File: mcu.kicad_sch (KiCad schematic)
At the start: 17 parts, among them J2 Conn_ARM_SWD_TagConnect_TC2030, U3 STM32L053R8Tx

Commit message: Added plugged in detection
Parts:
- added R39: 10M, Resistor_SMD:R_0402_1005Metric, symbol Device:R
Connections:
- net VDD: now also R39.1
- net SOLAR_PLUG: now reaches U3.27 (PB1)
- net SOLAR_PLUG: now also R39.2
- no-connect marks 34 -> 33
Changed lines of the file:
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@@
+	)
+	(junction
+		(at 193.04 96.52)
+		(diameter 0)
+		(color 0 0 0 0)
 	)
 	(junction
@@
 	)
 	(no_connect
-		(at 158.75 96.52)
-	)
-	(no_connect
 		(at 68.58 41.91)
 	)
@@
 	(wire
 		(pts
+			(xy 158.75 96.52) (xy 193.04 96.52)
+		)
+		(stroke
+			(width 0)
+			(type default)
+		)
+	)
+	(wire
+		(pts
 			(xy 165.1 121.92) (xy 158.75 121.92)
 		)
@@
 		(pts
 			(xy 250.19 26.67) (xy 256.54 26.67)
+		)
+		(stroke
+			(width 0)
+			(type default)
+		)
+	)
+	(wire
+		(pts
+			(xy 193.04 96.52) (xy 196.85 96.52)
 		)
 		(stroke
@@
 		(property "Intersheetrefs" "${INTERSHEET_REFS}"
 			(at 180.9667 53.34 0)
+			(effects
+				(font
+					(size 1.27 1.27)
+				)
+				(justify left)
+				(hide yes)
+			)
+		)
+	)
+	(global_label "SOLAR_PLUG"
+		(shape input)
+		(at 196.85 96.52 0)
+		(fields_autoplaced yes)
+		(effects
+			(font
+				(size 1.27 1.27)
+			)
+			(justify left)
+		)
+		(property "Intersheetrefs" "${INTERSHEET_REFS}"
+			(at 211.6281 96.52 0)
 			(effects
 				(font
@@
 	)
 	(symbol
+		(lib_id "Device:R")
+		(at 193.04 92.71 0)
+		(unit 1)
+		(exclude_from_sim no)
+		(in_bom yes)
+		(on_board yes)
+		(dnp no)
+		(fields_autoplaced yes)
+		(property "Reference" "R39"
+			(at 195.58 91.4399 0)
+			(effects
+				(font
+					(size 1.27 1.27)
+				)
+				(justify left)
+			)
+		)
+		(property "Value" "10M"
+			(at 195.58 93.9799 0)
+			(effects
+				(font
+					(size 1.27 1.27)
+				)
+				(justify left)
+			)
+		)
+		(property "Footprint" "Resistor_SMD:R_0402_1005Metric"
+			(at 191.262 92.71 90)
+			(effects
+				(font
+					(size 1.27 1.27)
+				)
+				(hide yes)
+			)
+		)
+		(property "Datasheet" "~"
+			(at 193.04 92.71 0)
+			(effects
+				(font
+					(size 1.27 1.27)
+				)
+				(hide yes)
+			)
+		)
+		(property "Description" "Resistor"
+			(at 193.04 92.71 0)
+			(effects
+				(font
+					(size 1.27 1.27)
+				)
+				(hide yes)
+			)
+		)
+		(pin "1"
+		)
+		(pin "2"
+		)
+		(instances
+			(project "JPBms2"
+				(path "/d86e471c-a8be-422d-a5d1-5a4699b7b766/852788cb-2266-4d4a-865c-a7e0873e4190"
+					(reference "R39")
+					(unit 1)
+				)
+			)
+		)
+	)
+	(symbol
 		(lib_id "power:PWR_FLAG")
 		(at 148.59 41.91 270)
@@
 					(unit 1)
 				)
+			)
+		)
+	)
+	(symbol
+		(lib_id "power:VDD")
+		(at 193.04 88.9 0)
+		(unit 1)
+		(exclude_from_sim no)
+		(in_bom yes)
+		(on_board yes)
+		(dnp no)
+		(fields_autoplaced yes)
+		(property "Reference" "#PWR053"
+			(at 193.04 92.71 0)
+			(effects
+				(font
+					(size 1.27 1.27)
+				)
+				(hide yes)
+			)
+		)
+		(property "Value" "VDD"
+			(at 193.04 83.82 0)
+			(effects
+				(font
+					(size 1.27 1.27)
+				)
+			)
+		)
+		(property "Footprint" ""
+			(at 193.04 88.9 0)
+			(effects
+				(font
+					(size 1.27 1.27)
+				)
+				(hide yes)
+			)
+		)
+		(property "Datasheet" ""
+			(at 193.04 88.9 0)
+			(effects
+				(font
+					(size 1.27 1.27)
+				)
+				(hide yes)
+			)
+		)
+		(property "Description" "Power symbol creates a global label with name \"VDD\""
+			(at 193.04 88.9 0)
+			(effects
+				(font
+					(size 1.27 1.27)
+				)
+				(hide yes)
+			)
+		)
+		(pin "1"
+		)
+		(instances
+			(project "JPBms2"
+				(path "/d86e471c-a8be-422d-a5d1-5a4699b7b766/852788cb-2266-4d4a-865c-a7e0873e4190"
+					(reference "#PWR053")
+					(unit 1)
+				)

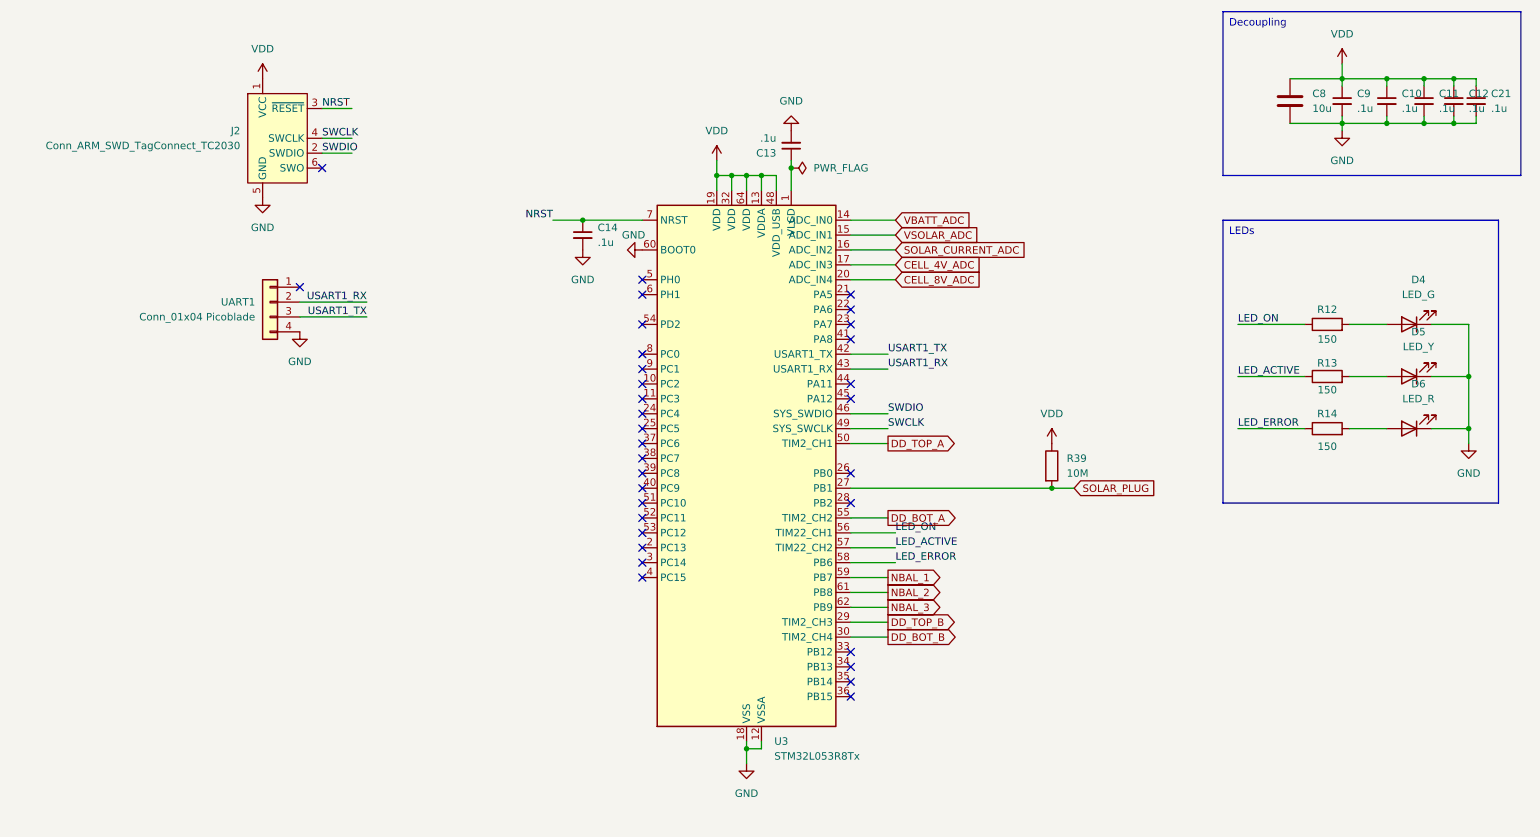
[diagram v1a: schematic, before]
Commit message: Adding a few notes, adding detection on solar and uart plugs
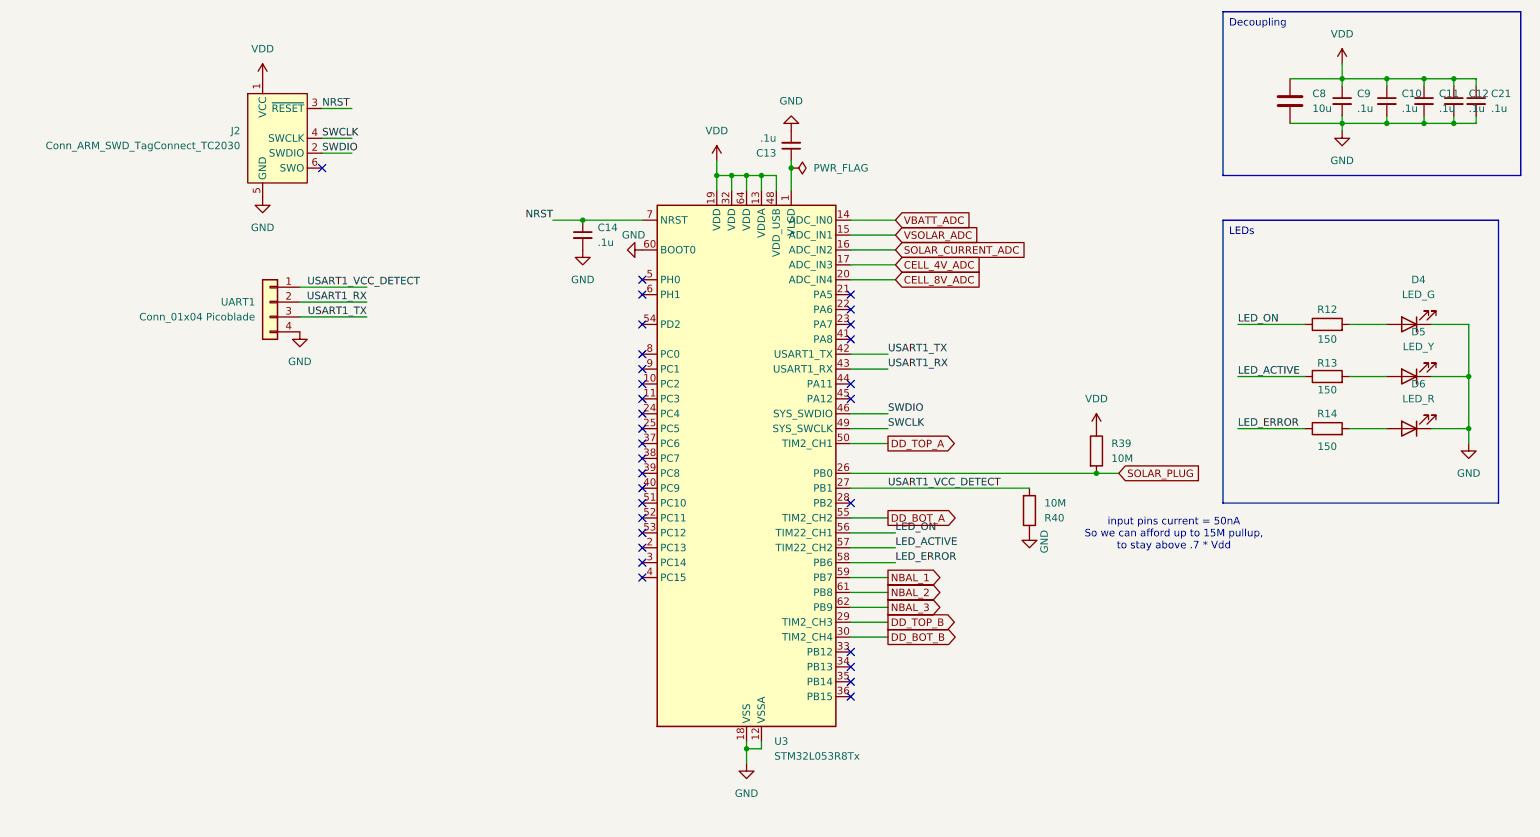
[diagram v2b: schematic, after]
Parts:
- added R40: 10M, Resistor_SMD:R_0402_1005Metric, symbol Device:R
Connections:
- net GND: now also R40.1
- net SOLAR_PLUG: now also U3.26 (PB0); no longer U3.27 (PB1)
- net USART1_VCC_DETECT: now reaches UART1.1 (Pin_1)
- net USART1_VCC_DETECT: now also U3.27 (PB1), R40.2
- no-connect marks 33 -> 31
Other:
- note added: "input pins current = 50nA So we can afford up to 15M pullup, to stay above .7 * Vdd"
- moved on the sheet: R39
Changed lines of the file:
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@@
 	)
 	(junction
+		(at 200.66 93.98)
+		(diameter 0)
+		(color 0 0 0 0)
+	)
+	(junction
 		(at 261.62 34.29)
 		(diameter 0)
@@
 	)
 	(junction
-		(at 193.04 96.52)
-		(diameter 0)
-		(color 0 0 0 0)
-	)
-	(junction
 		(at 148.59 41.91)
 		(diameter 0)
@@
 	)
 	(no_connect
-		(at 64.77 62.23)
-	)
-	(no_connect
 		(at 158.75 78.74)
 	)
@@
 	)
 	(no_connect
-		(at 158.75 93.98)
-	)
-	(no_connect
 		(at 123.19 104.14)
 	)
@@
 	(wire
 		(pts
-			(xy 158.75 96.52) (xy 193.04 96.52)
+			(xy 158.75 93.98) (xy 200.66 93.98)
 		)
 		(stroke
@@
 	(wire
 		(pts
+			(xy 64.77 62.23) (xy 76.2 62.23)
+		)
+		(stroke
+			(width 0)
+			(type default)
+		)
+	)
+	(wire
+		(pts
 			(xy 166.37 50.8) (xy 158.75 50.8)
 		)
@@
 	(wire
 		(pts
+			(xy 200.66 93.98) (xy 204.47 93.98)
+		)
+		(stroke
+			(width 0)
+			(type default)
+		)
+	)
+	(wire
+		(pts
 			(xy 68.58 36.83) (xy 73.66 36.83)
 		)
@@
 	(wire
 		(pts
-			(xy 193.04 96.52) (xy 196.85 96.52)
-		)
-		(stroke
-			(width 0)
-			(type default)
-		)
-	)
-	(wire
-		(pts
 			(xy 250.19 34.29) (xy 250.19 33.02)
 		)
@@
 	(wire
 		(pts
+			(xy 158.75 96.52) (xy 189.23 96.52)
+		)
+		(stroke
+			(width 0)
+			(type default)
+		)
+	)
+	(wire
+		(pts
 			(xy 76.2 67.31) (xy 64.77 67.31)
 		)
@@
 		)
 	)
+	(text "input pins current = 50nA \nSo we can afford up to 15M pullup,\nto stay above .7 * Vdd"
+		(exclude_from_sim no)
+		(at 213.868 104.394 0)
+		(effects
+			(font
+				(size 1.27 1.27)
+			)
+		)
+	)
 	(label "USART1_TX"
 		(at 76.2 67.31 180)
@@
 		)
 	)
+	(label "USART1_VCC_DETECT"
+		(at 165.1 96.52 0)
+		(fields_autoplaced yes)
+		(effects
+			(font
+				(size 1.27 1.27)
+			)
+			(justify left bottom)
+		)
+	)
 	(label "LED_ERROR"
 		(at 166.37 109.22 0)
@@
 		)
 	)
+	(label "USART1_VCC_DETECT"
+		(at 66.04 62.23 0)
+		(fields_autoplaced yes)
+		(effects
+			(font
+				(size 1.27 1.27)
+			)
+			(justify left bottom)
+		)
+	)
 	(label "NRST"
 		(at 107.95 50.8 180)
@@
 	(global_label "SOLAR_PLUG"
 		(shape input)
-		(at 196.85 96.52 0)
+		(at 204.47 93.98 0)
 		(fields_autoplaced yes)
 		(effects
@@
 		)
 		(property "Intersheetrefs" "${INTERSHEET_REFS}"
-			(at 211.6281 96.52 0)
+			(at 219.2481 93.98 0)
 			(effects
 				(font
@@
 	)
 	(symbol
+		(lib_id "power:GND")
+		(at 189.23 104.14 0)
+		(mirror y)
+		(unit 1)
+		(exclude_from_sim no)
+		(in_bom yes)
+		(on_board yes)
+		(dnp no)
+		(property "Reference" "#PWR054"
+			(at 189.23 110.49 0)
+			(effects
+				(font
+					(size 1.27 1.27)
+				)
+				(hide yes)
+			)
+		)
+		(property "Value" "GND"
+			(at 191.77 103.632 90)
+			(effects
+				(font
+					(size 1.27 1.27)
+				)
+				(justify right)
+			)
+		)
+		(property "Footprint" ""
+			(at 189.23 104.14 0)
+			(effects
+				(font
+					(size 1.27 1.27)
+				)
+				(hide yes)
+			)
+		)
+		(property "Datasheet" ""
+			(at 189.23 104.14 0)
+			(effects
+				(font
+					(size 1.27 1.27)
+				)
+				(hide yes)
+			)
+		)
+		(property "Description" "Power symbol creates a global label with name \"GND\" , ground"
+			(at 189.23 104.14 0)
+			(effects
+				(font
+					(size 1.27 1.27)
+				)
+				(hide yes)
+			)
+		)
+		(pin "1"
+		)
+		(instances
+			(project "JPBms2"
+				(path "/d86e471c-a8be-422d-a5d1-5a4699b7b766/852788cb-2266-4d4a-865c-a7e0873e4190"
+					(reference "#PWR054")
+					(unit 1)
+				)
+			)
+		)
+	)
+	(symbol
 		(lib_id "Device:C")
 		(at 233.68 30.48 0)
@@
 	(symbol
 		(lib_id "Device:R")
-		(at 193.04 92.71 0)
+		(at 200.66 90.17 0)
 		(unit 1)
 		(exclude_from_sim no)
@@
 		(fields_autoplaced yes)
 		(property "Reference" "R39"
-			(at 195.58 91.4399 0)
+			(at 203.2 88.8999 0)
 			(effects
 				(font
@@
 		)
 		(property "Value" "10M"
-			(at 195.58 93.9799 0)
+			(at 203.2 91.4399 0)
 			(effects
 				(font
@@
 		)
 		(property "Footprint" "Resistor_SMD:R_0402_1005Metric"
-			(at 191.262 92.71 90)
+			(at 198.882 90.17 90)
 			(effects
 				(font
@@
 		)
 		(property "Datasheet" "~"
-			(at 193.04 92.71 0)
+			(at 200.66 90.17 0)
 			(effects
 				(font
@@
 		)
 		(property "Description" "Resistor"
-			(at 193.04 92.71 0)
+			(at 200.66 90.17 0)
 			(effects
 				(font
@@
 	(symbol
 		(lib_id "power:VDD")
-		(at 193.04 88.9 0)
+		(at 200.66 86.36 0)
 		(unit 1)
 		(exclude_from_sim no)
@@
 		(fields_autoplaced yes)
 		(property "Reference" "#PWR053"
-			(at 193.04 92.71 0)
+			(at 200.66 90.17 0)
 			(effects
 				(font
@@
 		)
 		(property "Value" "VDD"
-			(at 193.04 83.82 0)
+			(at 200.66 81.28 0)
 			(effects
 				(font
@@
 		)
 		(property "Footprint" ""
-			(at 193.04 88.9 0)
+			(at 200.66 86.36 0)
 			(effects
 				(font
@@
 		)
 		(property "Datasheet" ""
-			(at 193.04 88.9 0)
+			(at 200.66 86.36 0)
 			(effects
 				(font
@@
 		)
 		(property "Description" "Power symbol creates a global label with name \"VDD\""
-			(at 193.04 88.9 0)
+			(at 200.66 86.36 0)
 			(effects
 				(font
@@
 					(unit 1)
 				)
+			)
+		)
+	)
+	(symbol
+		(lib_id "Device:R")
+		(at 189.23 100.33 0)
+		(mirror x)
+		(unit 1)
+		(exclude_from_sim no)
+		(in_bom yes)
+		(on_board yes)
+		(dnp no)
+		(fields_autoplaced yes)
+		(property "Reference" "R40"
+			(at 191.77 101.6001 0)
+			(effects
+				(font
+					(size 1.27 1.27)
+				)
+				(justify left)
+			)
+		)
+		(property "Value" "10M"
+			(at 191.77 99.0601 0)
+			(effects
+				(font
+					(size 1.27 1.27)
+				)
+				(justify left)
+			)
+		)
+		(property "Footprint" "Resistor_SMD:R_0402_1005Metric"
+			(at 187.452 100.33 90)
+			(effects
+				(font
+					(size 1.27 1.27)
+				)
+				(hide yes)
+			)
+		)
+		(property "Datasheet" "~"
+			(at 189.23 100.33 0)
+			(effects
+				(font
+					(size 1.27 1.27)
+				)
+				(hide yes)
+			)
+		)
+		(property "Description" "Resistor"
+			(at 189.23 100.33 0)
+			(effects
+				(font
+					(size 1.27 1.27)
+				)
+				(hide yes)
+			)
+		)
+		(pin "1"
+		)
+		(pin "2"
+		)
+		(instances
+			(project "JPBms2"
+				(path "/d86e471c-a8be-422d-a5d1-5a4699b7b766/852788cb-2266-4d4a-865c-a7e0873e4190"
+					(reference "R40")
+					(unit 1)
+				)

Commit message: Adding flow chart to main.c Adding leds on balancers
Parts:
- R12, R13, R14: footprint Resistor_SMD:R_0603_1608Metric -> Resistor_SMD:R_0402_1005Metric; LCSC_Code C22808 -> C25082
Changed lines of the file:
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@@
 			)
 		)
-		(property "Footprint" "Resistor_SMD:R_0603_1608Metric"
+		(property "Footprint" "Resistor_SMD:R_0402_1005Metric"
 			(at 240.03 88.138 90)
 			(effects
@@
 			)
 		)
-		(property "LCSC_Code" "C22808"
+		(property "LCSC_Code" "C25082"
 			(at 240.03 86.36 0)
 			(effects
@@
 			)
 		)
-		(property "Footprint" "Resistor_SMD:R_0603_1608Metric"
+		(property "Footprint" "Resistor_SMD:R_0402_1005Metric"
 			(at 240.03 70.358 90)
 			(effects
@@
 			)
 		)
-		(property "LCSC_Code" "C22808"
+		(property "LCSC_Code" "C25082"
 			(at 240.03 68.58 0)
 			(effects
@@
 			)
 		)
-		(property "Footprint" "Resistor_SMD:R_0603_1608Metric"
+		(property "Footprint" "Resistor_SMD:R_0402_1005Metric"
 			(at 240.03 79.248 90)
 			(effects
@@
 			)
 		)
-		(property "LCSC_Code" "C22808"
+		(property "LCSC_Code" "C25082"
 			(at 240.03 77.47 0)
 			(effects

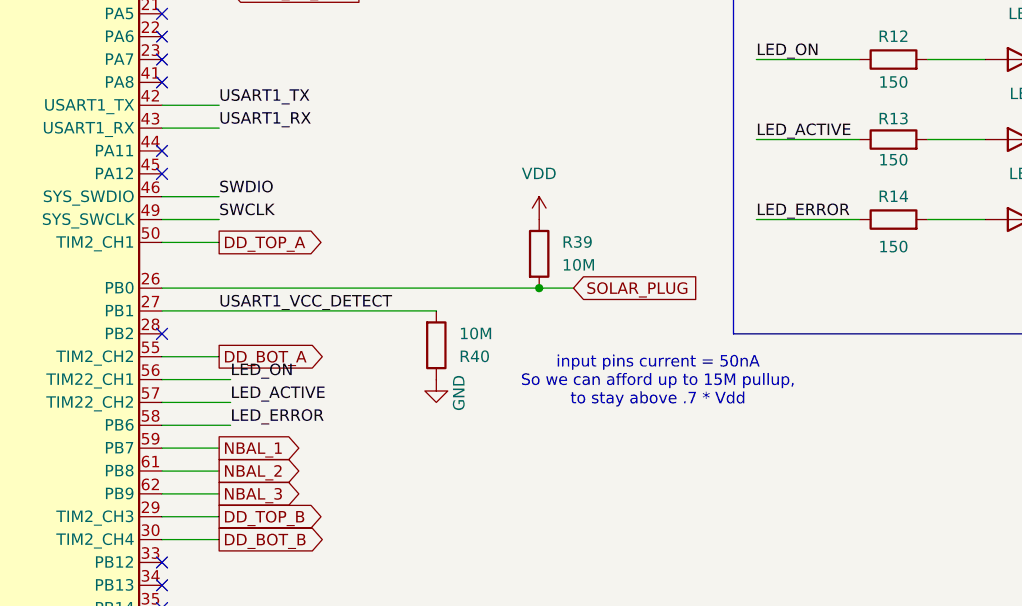
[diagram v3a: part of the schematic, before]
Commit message: Save power with usart, add oversampling support when balancing to get better reading, add notes on pcb
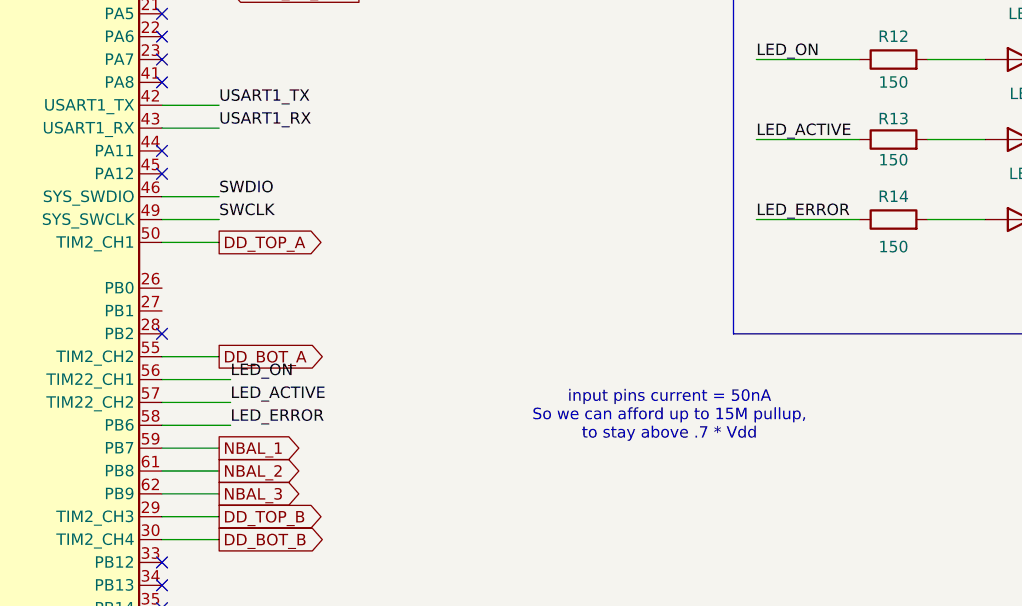
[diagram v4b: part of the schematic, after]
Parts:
- removed R39, R40: 10M, Resistor_SMD:R_0402_1005Metric, symbol Device:R
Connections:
- net USART1_VCC_DETECT: no longer U3.27 (PB1)
- net SOLAR_PLUG: no longer names the net of U3.26 (PB0)
